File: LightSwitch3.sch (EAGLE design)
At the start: 7 parts, among them SW1 SWITCH-SPST-ILLUMINATED, SW2 SWITCH-SPST-ILLUMINATED, SW3 SWITCH-SPST-ILLUMINATED

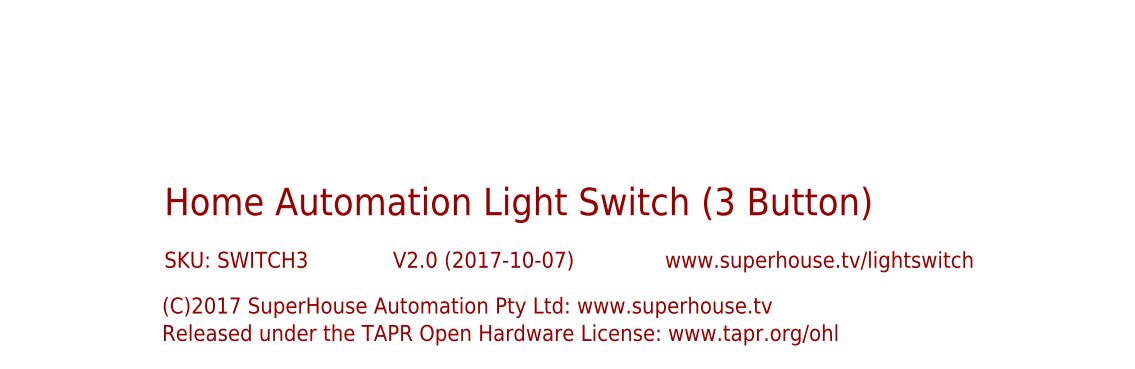
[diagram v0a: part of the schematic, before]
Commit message: Changed button footprint to slotted version for v2.1 release
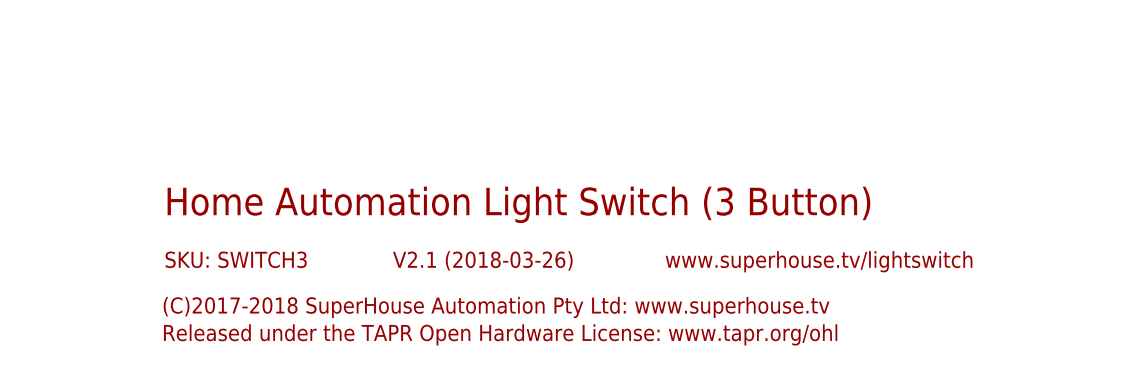
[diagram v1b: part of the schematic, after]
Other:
- note added: "(C)2017-2018 SuperHouse Automation Pty Ltd: www.superhouse.tv"
- note added: "V2.1 (2018-03-26)"
- note removed: "(C)2017 SuperHouse Automation Pty Ltd: www.superhouse.tv"
- note removed: "V2.0 (2017-10-07)"
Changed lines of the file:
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@@
 <?xml version="1.0" encoding="utf-8"?>
 <!DOCTYPE eagle SYSTEM "eagle.dtd">
-<eagle version="8.3.2">
+<eagle version="8.7.0">
 <drawing>
 <settings>
-<setting alwaysvectorfont="yes"/>
+<setting alwaysvectorfont="no"/>
 <setting keepoldvectorfont="yes"/>
 <setting verticaltext="up"/>
@@
 <layer number="60" name="p_dimension" color="6" fill="0" visible="no" active="no"/>
 <layer number="61" name="pt_docu" color="7" fill="0" visible="no" active="no"/>
+<layer number="88" name="SimResults" color="9" fill="1" visible="yes" active="yes"/>
+<layer number="89" name="SimProbes" color="9" fill="1" visible="yes" active="yes"/>
 <layer number="90" name="Modules" color="7" fill="1" visible="yes" active="yes"/>
 <layer number="91" name="Nets" color="2" fill="1" visible="yes" active="yes"/>
@@
 <frame x1="0" y1="0" x2="248.92" y2="185.42" columns="8" rows="5" layer="94"/>
 <text x="139.7" y="20.32" size="3.048" layer="94">Home Automation Light Switch (3 Button)</text>
-<text x="165.1" y="14.478" size="1.778" layer="94">V2.0 (2017-10-07)</text>
+<text x="165.1" y="14.478" size="1.778" layer="94">V2.1 (2018-03-26)</text>
 <text x="139.7" y="14.478" size="1.778" layer="94">SKU: SWITCH3</text>
-<text x="139.446" y="9.398" size="1.778" layer="94">(C)2017 SuperHouse Automation Pty Ltd: www.superhouse.tv</text>
+<text x="139.446" y="9.398" size="1.778" layer="94">(C)2017-2018 SuperHouse Automation Pty Ltd: www.superhouse.tv</text>
 <text x="139.446" y="6.35" size="1.778" layer="94">Released under the TAPR Open Hardware License: www.tapr.org/ohl</text>
 <text x="195.326" y="14.478" size="1.778" layer="94">www.superhouse.tv/lightswitch</text>

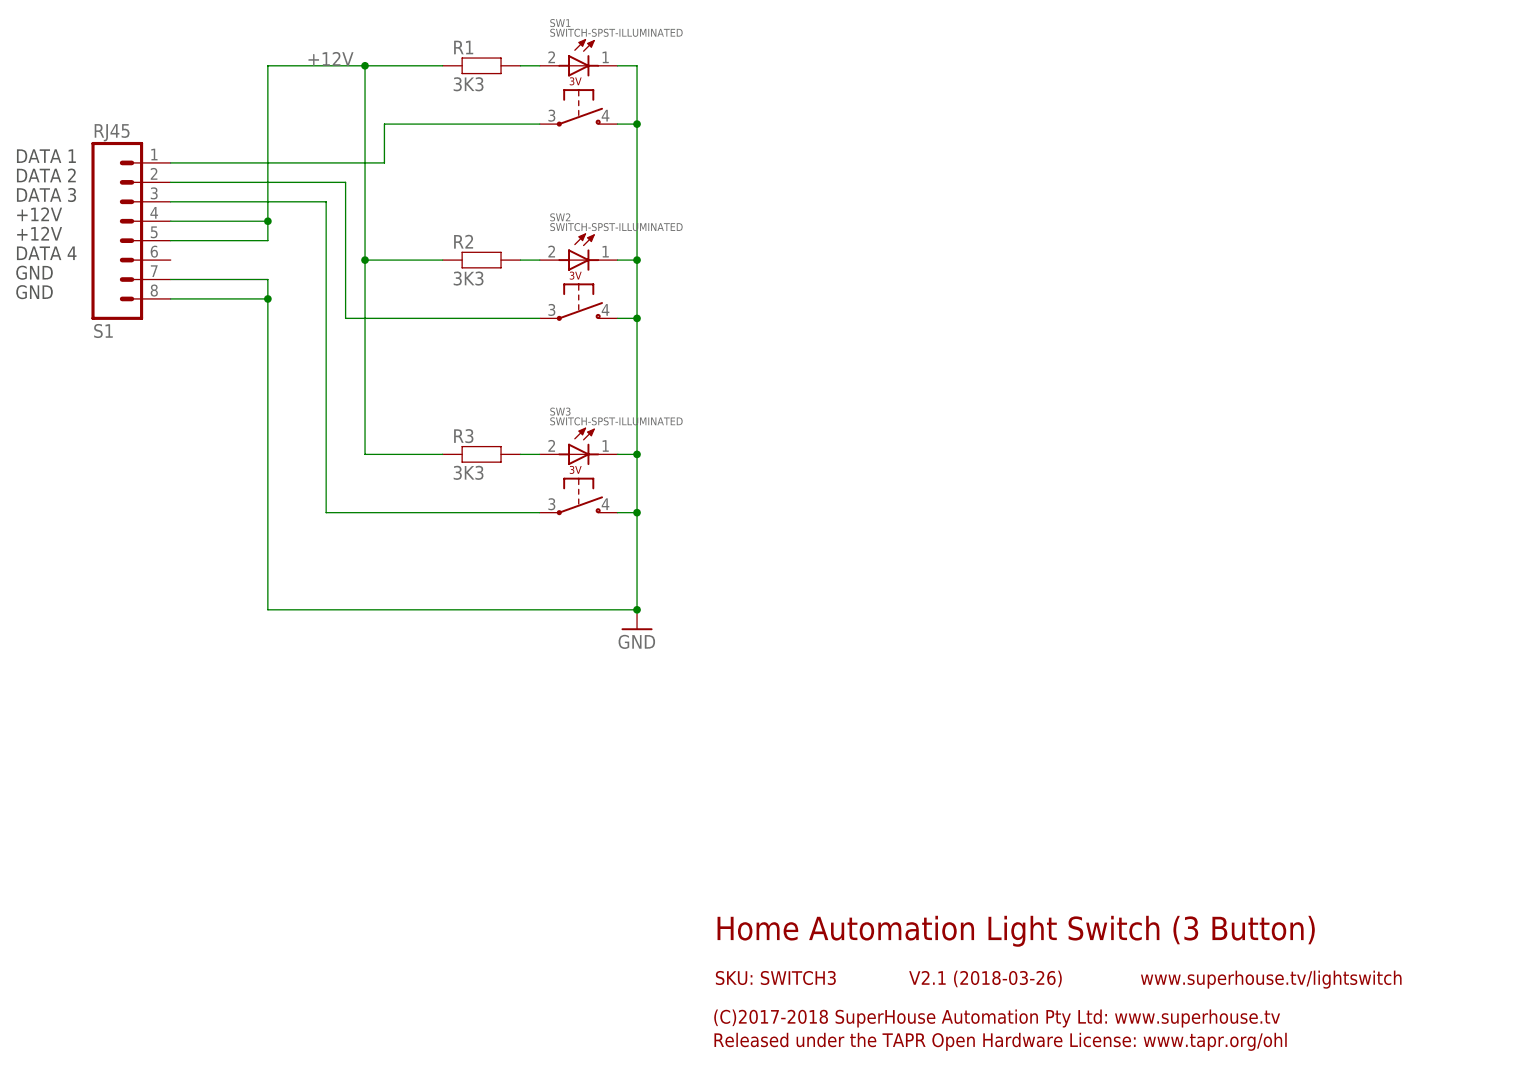
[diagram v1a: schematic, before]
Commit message: Updated RJ45 footprint for v2.2
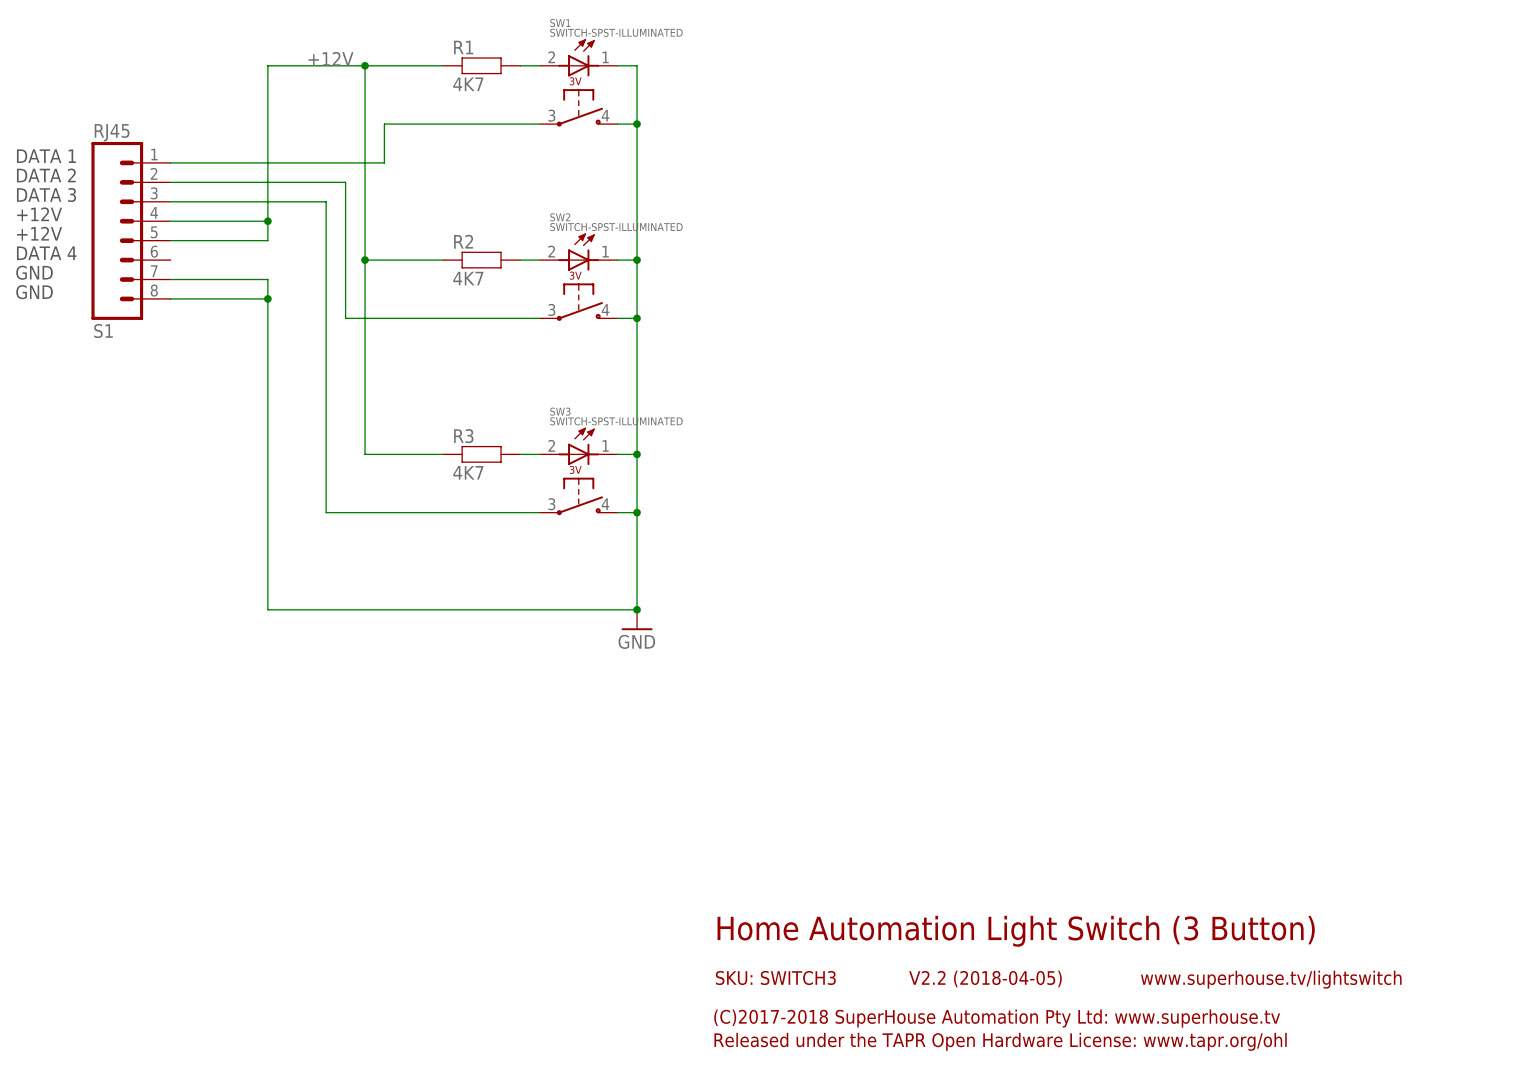
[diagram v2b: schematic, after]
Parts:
- R1, R2, R3: value 3K3 -> 4K7
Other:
- note added: "V2.2 (2018-04-05)"
- note removed: "V2.1 (2018-03-26)"
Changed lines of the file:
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@@
 <part name="GND3" library="SparkFun" deviceset="GND" device=""/>
 <part name="S1" library="freetronics-jon" deviceset="RJ45" device=""/>
-<part name="R1" library="freetronics-jon" deviceset="RESISTOR" device="0603" value="3K3"/>
-<part name="R2" library="freetronics-jon" deviceset="RESISTOR" device="0603" value="3K3"/>
-<part name="R3" library="freetronics-jon" deviceset="RESISTOR" device="0603" value="3K3"/>
+<part name="R1" library="freetronics-jon" deviceset="RESISTOR" device="0603" value="4K7"/>
+<part name="R2" library="freetronics-jon" deviceset="RESISTOR" device="0603" value="4K7"/>
+<part name="R3" library="freetronics-jon" deviceset="RESISTOR" device="0603" value="4K7"/>
 <part name="SW1" library="freetronics-jon" deviceset="SWITCH-SPST-ILLUMINATED" device=""/>
 <part name="SW2" library="freetronics-jon" deviceset="SWITCH-SPST-ILLUMINATED" device=""/>
@@
 <frame x1="0" y1="0" x2="248.92" y2="185.42" columns="8" rows="5" layer="94"/>
 <text x="139.7" y="20.32" size="3.048" layer="94">Home Automation Light Switch (3 Button)</text>
-<text x="165.1" y="14.478" size="1.778" layer="94">V2.1 (2018-03-26)</text>
+<text x="165.1" y="14.478" size="1.778" layer="94">V2.2 (2018-04-05)</text>
 <text x="139.7" y="14.478" size="1.778" layer="94">SKU: SWITCH3</text>
 <text x="139.446" y="9.398" size="1.778" layer="94">(C)2017-2018 SuperHouse Automation Pty Ltd: www.superhouse.tv</text>
